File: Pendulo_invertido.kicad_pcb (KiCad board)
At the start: 2 copper layers, 8 parts, among them IC2 MPU-6050, J3 Conn_01x02, J5 Conn_01x02, U2 TB6612FNG, U3 LM7805_TO220, U4 ESP32-devkitc

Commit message: Cambios huellas y pcb
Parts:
- removed IC2: MPU-6050, Library:MPU-6050
- removed U4: ESP32-devkitc, Library:ESP32-devkitc-v4
- added IC1: MPU-6050, Library:MPU6050, F.Cu at (160.3, 69.6)
- added J1: Conn_01x02, TerminalBlock_Phoenix:TerminalBlock_Phoenix_MKDS-1,5-2-5.08_1x02_P5.08mm_Horizontal, F.Cu at (189.0, 120.4)
- added REF**: MountingHole_3.2mm_M3, MountingHole:MountingHole_3.2mm_M3, F.Cu at (106.7, 144.8)
- added REF**: MountingHole_3.2mm_M3, MountingHole:MountingHole_3.2mm_M3, F.Cu at (208.3, 66.0)
- added REF**: MountingHole_3.2mm_M3, MountingHole:MountingHole_3.2mm_M3, F.Cu at (208.3, 144.8)
- added REF**: MountingHole_3.2mm_M3, MountingHole:MountingHole_3.2mm_M3, F.Cu at (106.7, 66.0)
- added U1: ESP32-devkitc, Library:ESP32-devkitc-v4, F.Cu at (126.5, 74.9)
- J3, J5: footprint Connector_JST:JST_XH_B2B-XH-A_1x02_P2.50mm_Vertical -> TerminalBlock_Phoenix:TerminalBlock_Phoenix_MKDS-1,5-2-5.08_1x02_P5.08mm_Horizontal
- moved U3 108.2 mm to (176.5, 125.0), turned to -90 degrees
- moved C1 106.2 mm to (171.0, 125.0), turned to 180 degrees
- moved C2 95.0 mm to (170.0, 130.5), turned to -90 degrees
- moved U2 91.6 mm to (173.1, 111.3), turned to 180 degrees
- moved J5 73.8 mm to (193.8, 95.0), turned to 90 degrees
- moved J3 43.7 mm to (113.7, 92.5), turned to -90 degrees
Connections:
- C1 pad 1: +6V -> Net-(J1-Pin_2)
- U2 pad 1: (no net) -> Net-(J1-Pin_2)
- U2 pad 10: (no net) -> PWMB
- U2 pad 11: (no net) -> BIN2
- U2 pad 12: (no net) -> BIN1
- U2 pad 13: (no net) -> STBY
- U2 pad 14: (no net) -> AIN1
- U2 pad 15: (no net) -> AIN2
- U2 pad 16: (no net) -> PWMA
- U2 pad 2: (no net) -> Net-(IC1-VCC)
- U2 pad 3: (no net) -> GND
- U2 pad 4: (no net) -> A01
- U2 pad 5: (no net) -> A02
- U2 pad 6: (no net) -> B01
- U2 pad 7: (no net) -> B02
- U2 pad 8: (no net) -> GND
- U2 pad 9: (no net) -> GND
- U3 pad 1: +6V -> Net-(J1-Pin_2)
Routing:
- net A02: track 0.00 -> 195.5 mm
- net A01: track 0.00 -> 177.9 mm
- net PWMA: track 0.00 -> 125.5 mm, vias 0 -> 2
- net AIN2: track 0.00 -> 106.3 mm, vias 0 -> 2
- net Net-(IC1-VCC): track 0.00 -> 94.4 mm
- net STBY: track 0.00 -> 78.5 mm
- net AIN1: track 0.00 -> 74.6 mm
- net BIN1: track 0.00 -> 67.1 mm
- net Net-(U1-5V): track 0.00 -> 56.0 mm
- net BIN2: track 0.00 -> 53.7 mm
- net PWMB: track 0.00 -> 53.7 mm
- net Net-(J1-Pin_2): track 0.00 -> 37.7 mm
- net B02: track 0.00 -> 23.2 mm
- net B01: track 0.00 -> 22.0 mm
- net Net-(IC1-SDA): track 0.00 -> 17.0 mm
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- added copper zone on B.Cu, net GND
- added copper zone on F.Cu, net GND
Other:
- board outline added: 111.8 x 88.9 mm
- board text added: "Manu Ourille"

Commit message: Ultimos cambios y creacion archivos gerber
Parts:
- moved J1 16.8 mm to (205.7, 121.9)
- moved J5 13.6 mm to (205.7, 101.6)
- moved J3 5.18 mm to (111.3, 97.0)
- moved REF** 2.54 mm to (109.2, 144.8)
- moved REF** 2.54 mm to (109.2, 66.0)
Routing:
- net A02: track 195.5 -> 177.3 mm
- net Net-(J1-Pin_2): track 37.7 -> 55.1 mm, vias 0 -> 2
- net PWMB: track 53.7 -> 69.7 mm
- net A01: track 177.9 -> 162.6 mm
- net B02: track 23.2 -> 37.8 mm
- net B01: track 22.0 -> 36.6 mm
- net BIN2: track 53.7 -> 65.1 mm, vias 0 -> 2
- net STBY: track 78.5 -> 80.9 mm
- net BIN1: track 67.1 -> 67.9 mm
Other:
- board size 111.8 x 88.9 mm -> 108.7 x 88.9 mm

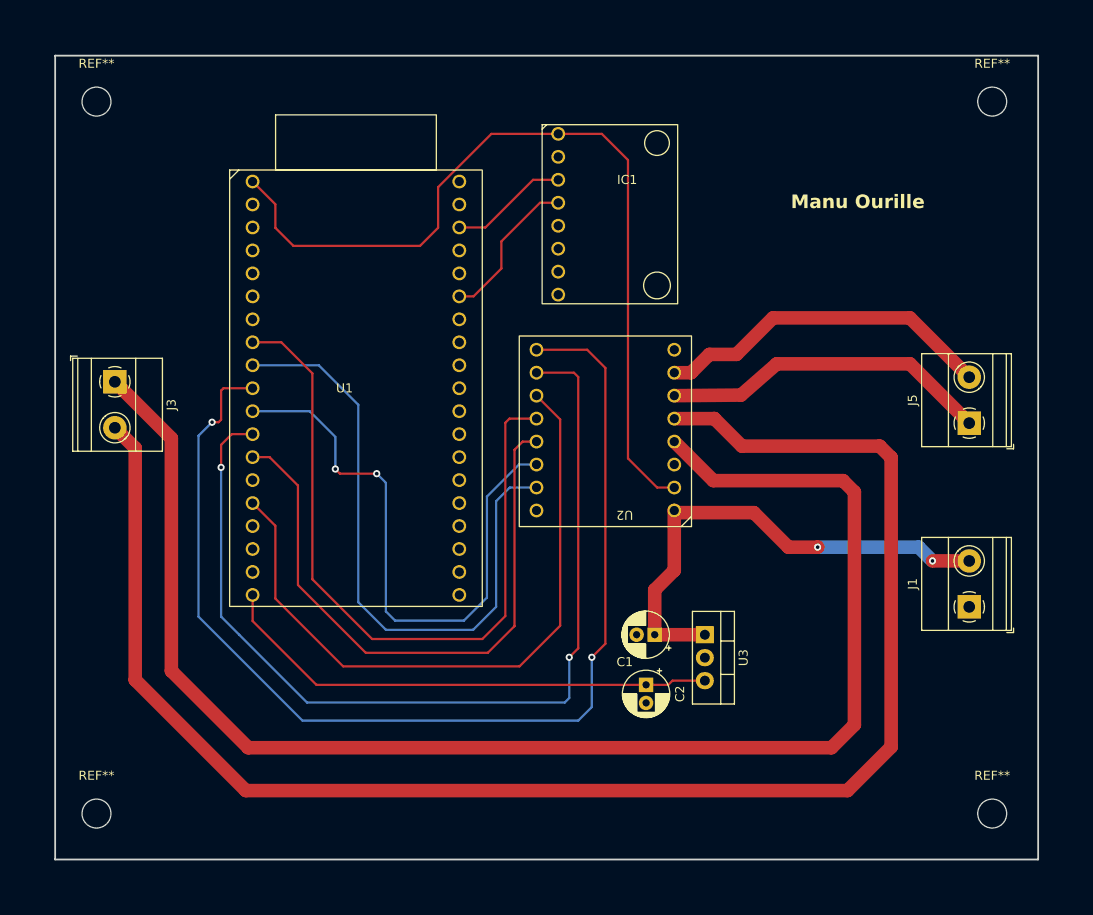
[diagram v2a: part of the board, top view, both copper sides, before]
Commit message: Resolucion error de medidas
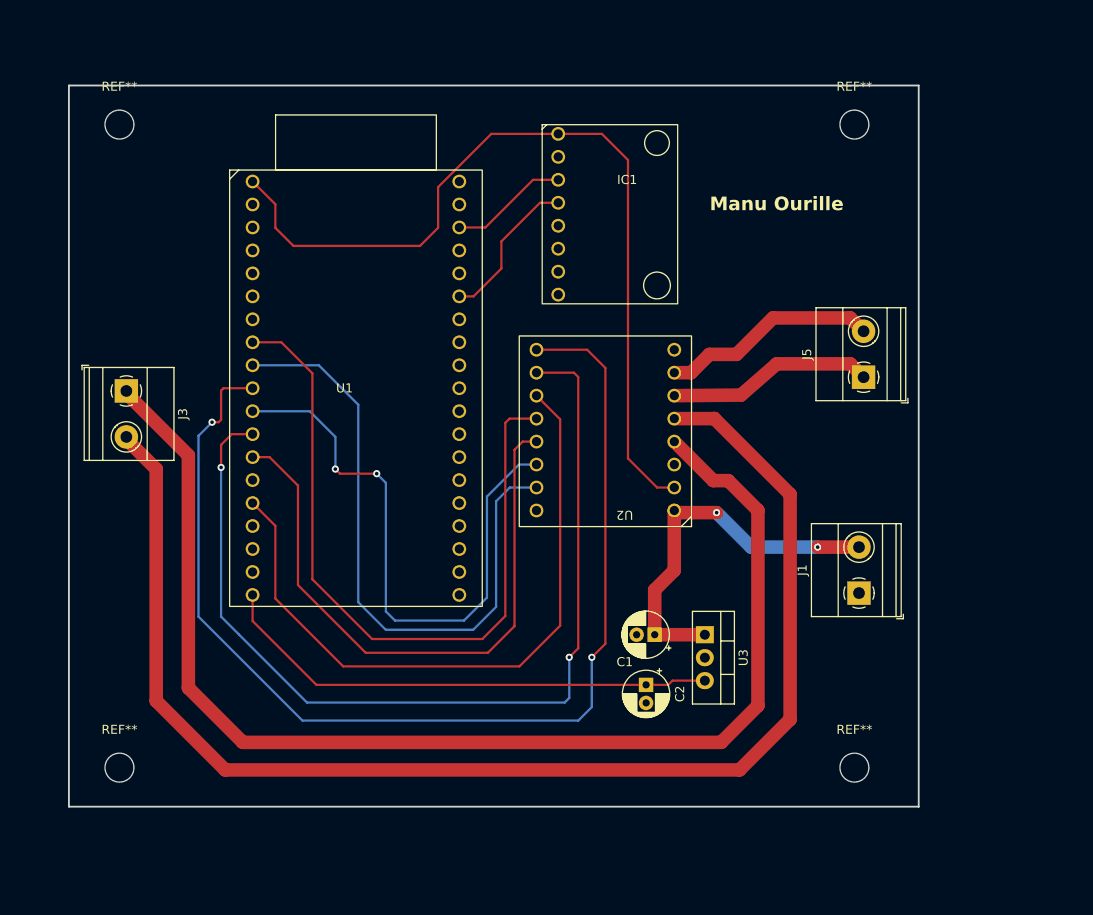
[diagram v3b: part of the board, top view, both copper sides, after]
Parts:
- moved REF** 16.1 mm to (193.0, 139.7)
- moved REF** 15.5 mm to (193.0, 68.6)
- moved J5 12.7 mm to (194.1, 96.5)
- moved J1 12.3 mm to (193.5, 120.4)
- moved REF** 5.68 mm to (111.8, 139.7)
- moved REF** 3.59 mm to (111.8, 68.6)
- moved J3 1.63 mm to (112.5, 98.0)
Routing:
- net A02: track 177.3 -> 147.3 mm
- net A01: track 162.6 -> 136.8 mm
- net B02: track 37.8 -> 24.1 mm
- net B01: track 36.6 -> 22.8 mm
- net Net-(J1-Pin_2): track 55.1 -> 42.3 mm
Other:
- board size 108.7 x 88.9 mm -> 94 x 79.8 mm
